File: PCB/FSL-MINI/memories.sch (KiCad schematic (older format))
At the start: 27 parts, among them J1001 SD CARD, Q1001 FDN340P, U1001 S25FL032P0XMFI013, U1002 24AA1025, U1003 24AA025E48

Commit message: Primer recorte realizado con Esteban Volentini <evolentini@gmail.com>.
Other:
- note added: "AVERIGUAR PROPOSITO"
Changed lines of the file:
@@
 $Descr A4 11693 8268
 encoding utf-8
-Sheet 10 13
+Sheet 5 6
 Title "CIAA Memorias NV"
 Date "2 dec 2014"
@@
 	1    0    0    -1
 $EndComp
-Text Notes 2000 7250 0    60   ~ 0
+Text Notes 2000 7400 0    60   ~ 0
 Detección de la memoria: Como el zócalo \nno posee switch mecánico, se utiliza \nun cambio de nivel en la línea DAT3,\npara lo cual es necesario un pull down\n(el valor 750k es el recomendado por FSL).
 $Comp
@@
 Connection ~ 2900 5500
 Wire Notes Line
-	1950 7100 4050 7100
+	1950 6900 4050 6900
 Wire Notes Line
-	4050 7100 4050 7650
+	4050 6900 4050 7450
 Wire Notes Line
-	1950 7100 1950 7650
+	1950 6900 1950 7450
 Wire Notes Line
-	1950 7650 4050 7650
+	1950 7450 4050 7450
+Text Notes 3650 2900 0    60   ~ 0
+AVERIGUAR PROPOSITO
+Text Notes 8150 6350 0    60   ~ 0
+AVERIGUAR PROPOSITO
 $EndSCHEMATC

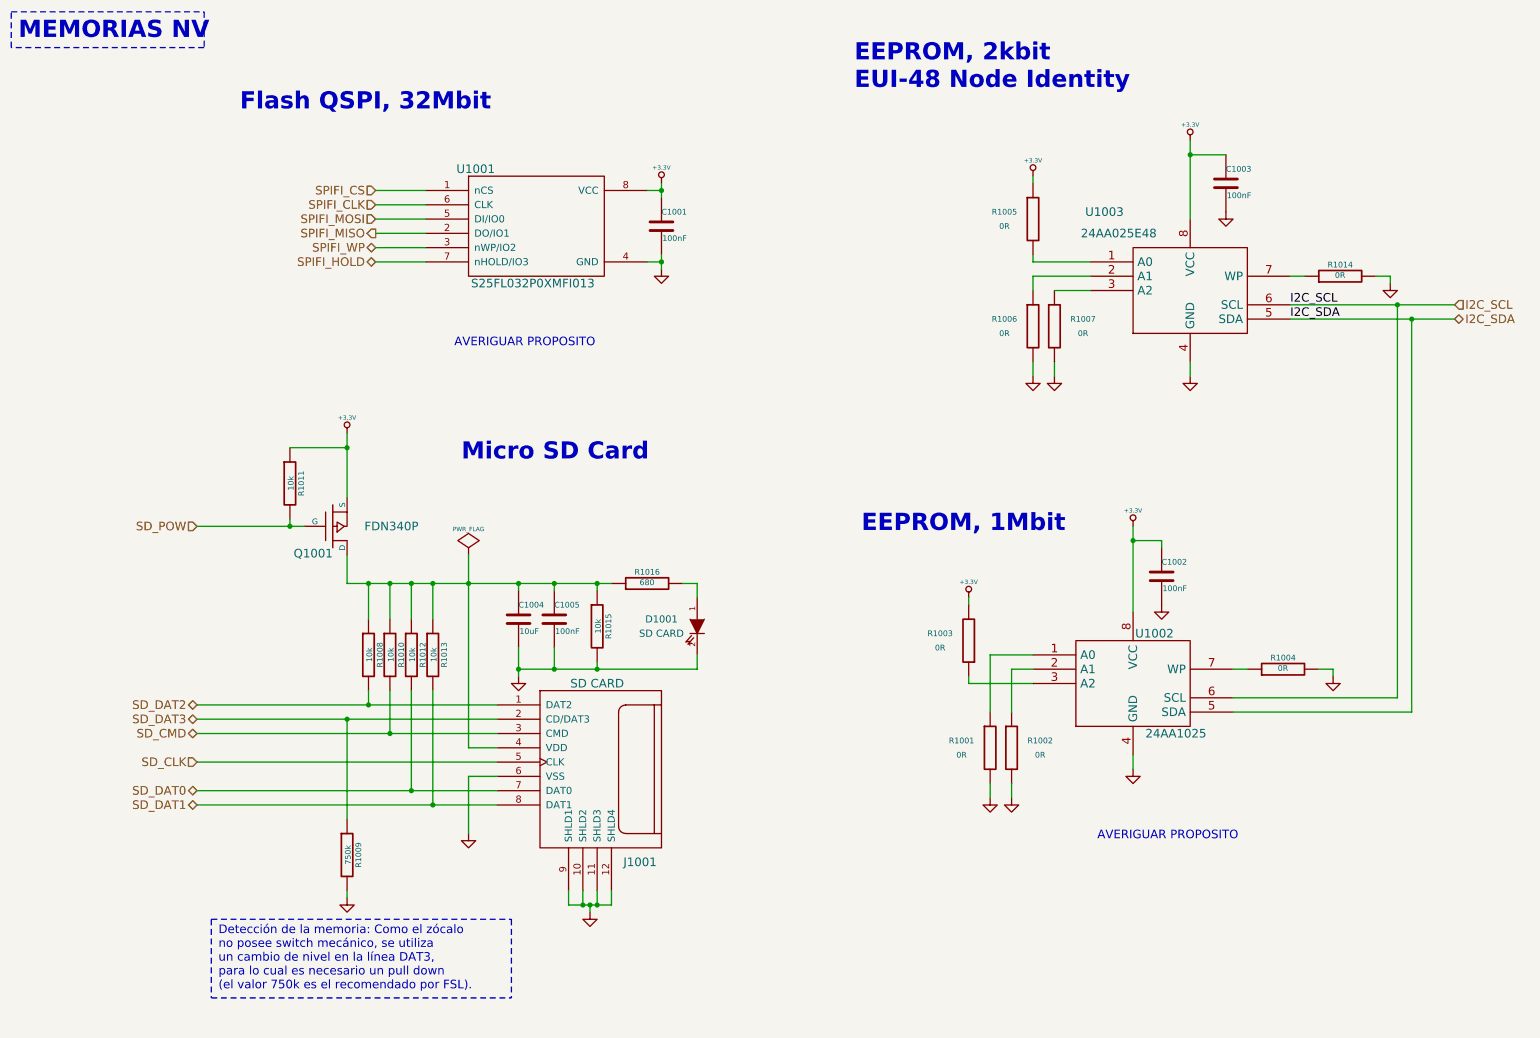
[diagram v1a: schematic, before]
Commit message: Added temporal connectors to avoid ERC.
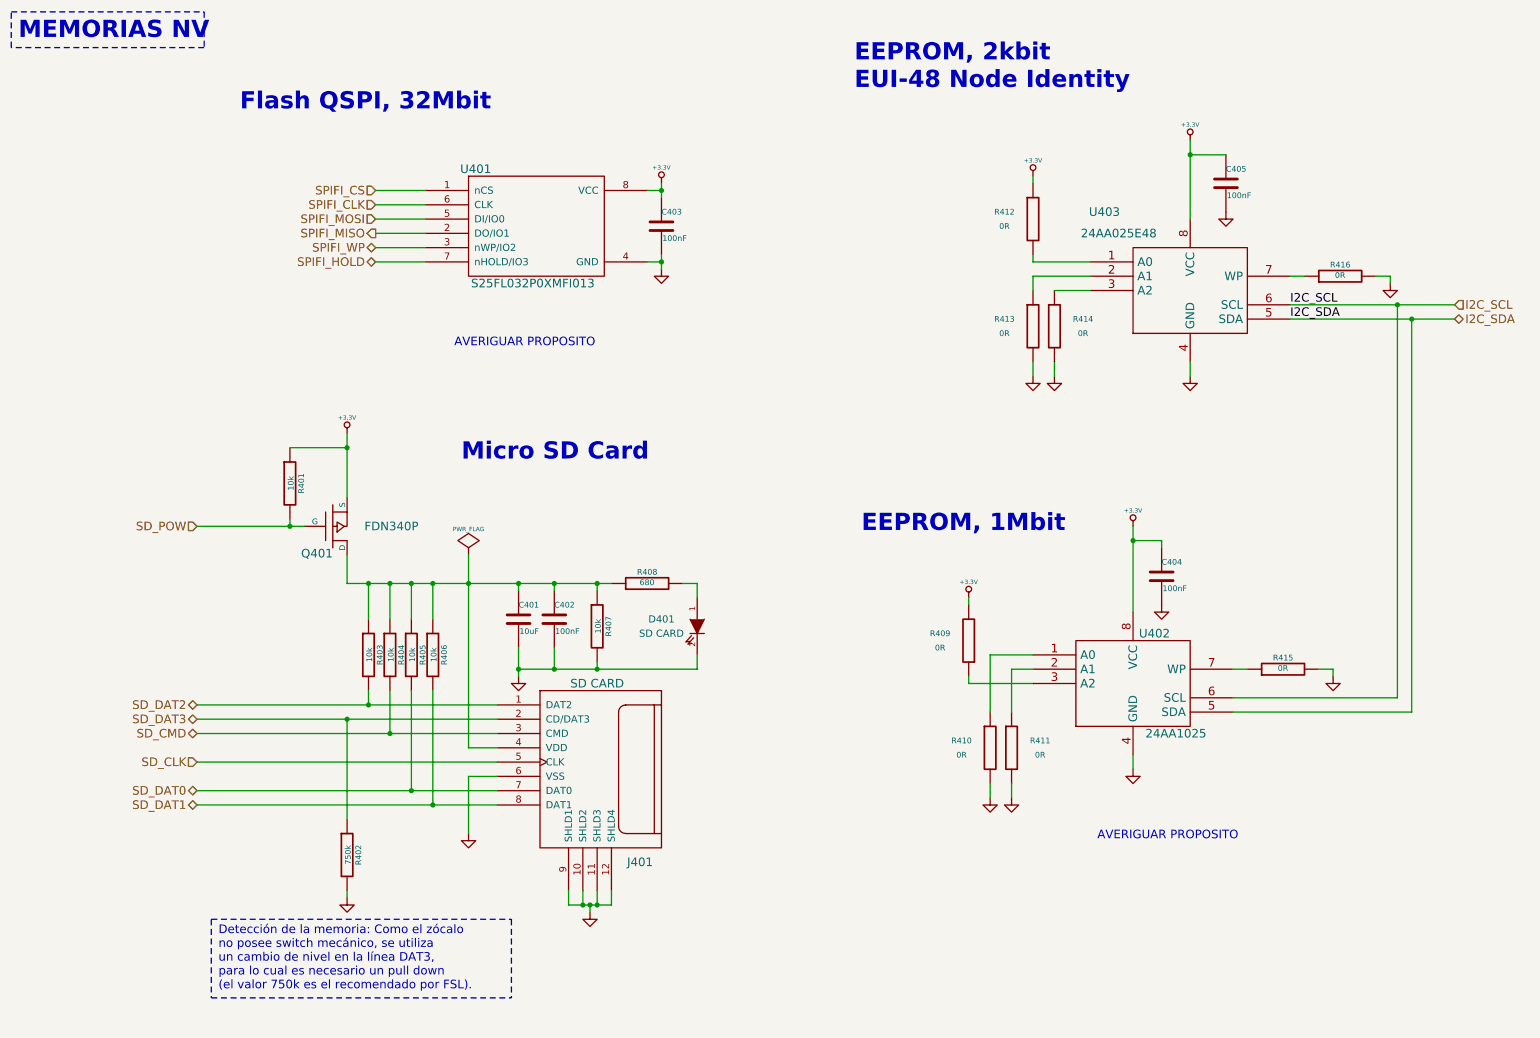
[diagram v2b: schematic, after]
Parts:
- renumbered C1004 to C401, C1005 to C402, C1001 to C403, C1002 to C404, C1003 to C405, D1001 to D401, J1001 to J401, Q1001 to Q401, R1011 to R401, R1009 to R402, R1008 to R403, R1010 to R404, R1012 to R405, R1013 to R406, R1015 to R407, R1016 to R408, R1003 to R409, R1001 to R410, R1002 to R411, R1005 to R412, R1006 to R413, R1007 to R414, R1004 to R415, R1014 to R416, U1001 to U401, U1002 to U402, U1003 to U403

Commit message: Footprint information in schematics.
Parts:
- C401: footprint c_1206POL -> footprints:c_1206POL
- C402, C403, C404, C405: footprint c_0603 -> footprints:c_0603
- D401: footprint LED-0603 -> footprints:LED-0603
- J401: footprint MicroSD_Hinged -> footprints:MicroSD_Hinged
- Q401: footprint SOT-23 -> footprints:SOT-23
- R401, R402, R403, R404, R405, R406, R407, R408, R409, R410, R411, R412, R413, R414, R415, R416: footprint r_0603 -> footprints:r_0603
- U401: footprint SOIC-8_WIDE -> footprints:SOIC-8_WIDE
- U402, U403: footprint SOIC-8 -> footprints:SOIC-8
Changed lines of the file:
@@
 F 0 "R403" V 3130 5050 40  0000 C CNN
 F 1 "10k" V 3057 5051 40  0000 C CNN
-F 2 "r_0603" H 3580 5050 30  0001 C CNN
+F 2 "footprints:r_0603" H 3580 5050 30  0001 C CNN
 F 3 "~" H 3650 5050 30  0000 C CNN
 F 4 "RES 10K OHM 1/10W 5% 0603 SMD" H 3650 5050 60  0001 C CNN "Descripcion"
@@
 F 0 "R404" V 3280 5050 40  0000 C CNN
 F 1 "10k" V 3207 5051 40  0000 C CNN
-F 2 "r_0603" H 3430 5050 30  0001 C CNN
+F 2 "footprints:r_0603" H 3430 5050 30  0001 C CNN
 F 3 "~" H 3500 5050 30  0000 C CNN
 F 4 "RES 10K OHM 1/10W 5% 0603 SMD" H 3500 5050 60  0001 C CNN "Descripcion"
@@
 F 0 "R405" V 3430 5050 40  0000 C CNN
 F 1 "10k" V 3357 5051 40  0000 C CNN
-F 2 "r_0603" H 3430 5050 30  0001 C CNN
+F 2 "footprints:r_0603" H 3430 5050 30  0001 C CNN
 F 3 "~" H 3500 5050 30  0000 C CNN
 F 4 "RES 10K OHM 1/10W 5% 0603 SMD" H 3500 5050 60  0001 C CNN "Descripcion"
@@
 F 0 "Q401" H 2800 4340 60  0000 R CNN
 F 1 "FDN340P" H 3400 4150 60  0000 R CNN
-F 2 "SOT-23" H 2800 4150 60  0001 C CNN
+F 2 "footprints:SOT-23" H 2800 4150 60  0001 C CNN
 F 3 "~" H 2800 4150 60  0000 C CNN
 F 4 "MOSFET P-CH 20V 2A SSOT3" H 2800 4150 60  0001 C CNN "Descripcion"
@@
 F 0 "R401" V 2580 3850 40  0000 C CNN
 F 1 "10k" V 2507 3851 40  0000 C CNN
-F 2 "r_0603" H 2580 4900 30  0001 C CNN
+F 2 "footprints:r_0603" H 2580 4900 30  0001 C CNN
 F 3 "~" H 2650 4900 30  0000 C CNN
 F 4 "RES 10K OHM 1/10W 5% 0603 SMD" H 2650 4900 60  0001 C CNN "Descripcion"
@@
 F 0 "R408" V 5080 4550 40  0000 C CNN
 F 1 "680" V 5007 4551 40  0000 C CNN
-F 2 "r_0603" V 4930 4550 30  0001 C CNN
+F 2 "footprints:r_0603" V 4930 4550 30  0001 C CNN
 F 3 "~" H 5000 4550 30  0000 C CNN
 F 4 "RES 680 OHM 1/10W 5% 0603 SMD" H 5000 4550 60  0001 C CNN "Descripcion"
@@
 F 0 "R407" V 4730 4850 40  0000 C CNN
 F 1 "10k" V 4657 4851 40  0000 C CNN
-F 2 "r_0603" H 3430 5050 30  0001 C CNN
+F 2 "footprints:r_0603" H 3430 5050 30  0001 C CNN
 F 3 "~" H 3500 5050 30  0000 C CNN
 F 4 "RES 10K OHM 1/10W 5% 0603 SMD" H 3500 5050 60  0001 C CNN "Descripcion"
@@
 F 0 "C402" H 4350 4900 40  0000 L CNN
 F 1 "100nF" H 4356 4715 40  0000 L CNN
-F 2 "c_0603" H 4388 4650 30  0001 C CNN
+F 2 "footprints:c_0603" H 4388 4650 30  0001 C CNN
 F 3 "~" H 4350 4800 60  0000 C CNN
 F 4 "CAP CER 0,1UF 16V 10% X7R 0603" H 4350 4800 60  0001 C CNN "Descripcion"
@@
 F 0 "C401" H 4100 4900 40  0000 L CNN
 F 1 "10uF" H 4106 4715 40  0000 L CNN
-F 2 "c_1206POL" H 4138 4650 30  0001 C CNN
+F 2 "footprints:c_1206POL" H 4138 4650 30  0001 C CNN
 F 3 "~" H 4100 4800 60  0000 C CNN
 F 4 "CAP TANT 10UF 6.3V 10% 1206" H 4100 4800 60  0001 C CNN "Descripcion"
@@
 F 0 "D401" V 5300 4600 50  0000 C CNN
 F 1 "SD CARD" V 5400 4600 50  0000 C CNN
-F 2 "LED-0603" H 5350 4850 60  0001 C CNN
+F 2 "footprints:LED-0603" H 5350 4850 60  0001 C CNN
 F 3 "~" H 5350 4850 60  0000 C CNN
 F 4 "LED GRN WATER CLEAR 0603 SMD" H 5350 4850 60  0001 C CNN "Descripcion"
@@
 F 0 "R406" V 3580 5050 40  0000 C CNN
 F 1 "10k" V 3507 5051 40  0000 C CNN
-F 2 "r_0603" H 3430 5050 30  0001 C CNN
+F 2 "footprints:r_0603" H 3430 5050 30  0001 C CNN
 F 3 "~" H 3500 5050 30  0000 C CNN
 F 4 "RES 10K OHM 1/10W 5% 0603 SMD" H 3500 5050 60  0001 C CNN "Descripcion"
@@
 F 0 "J401" H 4950 5300 60  0000 C CNN
 F 1 "SD CARD" H 4650 6550 60  0000 C CNN
-F 2 "MicroSD_Hinged" H 4650 5900 60  0001 C CNN
+F 2 "footprints:MicroSD_Hinged" H 4650 5900 60  0001 C CNN
 F 3 "~" H 4650 5900 60  0000 C CNN
 F 4 "CONN MEMORY CARD R/A 8POS SMD" H 4650 5900 60  0001 C CNN "Descripcion"
@@
 F 0 "U402" H 8550 5600 60  0000 C CNN
 F 1 "24AA1025" H 8700 4900 60  0000 C CNN
-F 2 "SOIC-8" H 8400 5250 60  0001 C CNN
+F 2 "footprints:SOIC-8" H 8400 5250 60  0001 C CNN
 F 3 "~" H 8400 5250 60  0000 C CNN
 F 4 "IC EEPROM 1MBIT 400KHZ 8SOIC" H 8400 5250 60  0001 C CNN "Descripcion"
@@
 F 0 "U403" H 8200 3050 60  0000 C CNN
 F 1 "24AA025E48" H 8300 2900 60  0000 C CNN
-F 2 "SOIC-8" H 8800 2500 60  0001 C CNN
+F 2 "footprints:SOIC-8" H 8800 2500 60  0001 C CNN
 F 3 "~" H 8800 2500 60  0000 C CNN
 F 4 "IC EEPROM 2KBIT 400KHZ 8SOIC" H 8800 2500 60  0001 C CNN "Descripcion"
@@
 F 0 "R411" H 7750 5750 40  0000 C CNN
 F 1 "0R" H 7750 5650 40  0000 C CNN
-F 2 "r_0603" V 11080 5800 30  0001 C CNN
+F 2 "footprints:r_0603" V 11080 5800 30  0001 C CNN
 F 3 "~" H 11150 5800 30  0000 C CNN
 F 4 "RES 0.0 OHM 1/10W JUMP 0603 SMD" H 11150 5800 60  0001 C CNN "Descripcion"
@@
 F 0 "R409" H 7450 4900 40  0000 C CNN
 F 1 "0R" H 7450 5000 40  0000 C CNN
-F 2 "r_0603" V 10630 5050 30  0001 C CNN
+F 2 "footprints:r_0603" V 10630 5050 30  0001 C CNN
 F 3 "~" H 10700 5050 30  0000 C CNN
 F 4 "RES 0.0 OHM 1/10W JUMP 0603 SMD" H 10700 5050 60  0001 C CNN "Descripcion"
@@
 F 0 "R410" H 7200 5750 40  0000 C CNN
 F 1 "0R" H 7200 5650 40  0000 C CNN
-F 2 "r_0603" V 11080 5800 30  0001 C CNN
+F 2 "footprints:r_0603" V 11080 5800 30  0001 C CNN
 F 3 "~" H 11150 5800 30  0000 C CNN
 F 4 "RES 0.0 OHM 1/10W JUMP 0603 SMD" H 11150 5800 60  0001 C CNN "Descripcion"
@@
 F 0 "R413" H 7500 2800 40  0000 C CNN
 F 1 "0R" H 7500 2700 40  0000 C CNN
-F 2 "r_0603" V 7780 2750 30  0001 C CNN
+F 2 "footprints:r_0603" V 7780 2750 30  0001 C CNN
 F 3 "~" H 7850 2750 30  0000 C CNN
 F 4 "RES 0.0 OHM 1/10W JUMP 0603 SMD" H 7850 2750 60  0001 C CNN "Descripcion"
@@
 F 0 "R414" H 8050 2800 40  0000 C CNN
 F 1 "0R" H 8050 2700 40  0000 C CNN
-F 2 "r_0603" V 7780 2750 30  0001 C CNN
+F 2 "footprints:r_0603" V 7780 2750 30  0001 C CNN
 F 3 "~" H 7850 2750 30  0000 C CNN
 F 4 "RES 0.0 OHM 1/10W JUMP 0603 SMD" H 7850 2750 60  0001 C CNN "Descripcion"
@@
 F 0 "R412" H 7500 2050 40  0000 C CNN
 F 1 "0R" H 7500 1950 40  0000 C CNN
-F 2 "r_0603" V 7930 2000 30  0001 C CNN
+F 2 "footprints:r_0603" V 7930 2000 30  0001 C CNN
 F 3 "~" H 8000 2000 30  0000 C CNN
 F 4 "RES 0.0 OHM 1/10W JUMP 0603 SMD" H 8000 2000 60  0001 C CNN "Descripcion"
@@
 F 0 "R415" V 9530 5150 40  0000 C CNN
 F 1 "0R" V 9457 5151 40  0000 C CNN
-F 2 "r_0603" V 11180 5850 30  0001 C CNN
+F 2 "footprints:r_0603" V 11180 5850 30  0001 C CNN
 F 3 "~" H 11250 5850 30  0001 C CNN
 F 4 "RES 0.0 OHM 1/10W JUMP 0603 SMD" H 11250 5850 60  0001 C CNN "Descripcion"
@@
 F 0 "R416" V 9930 2400 40  0000 C CNN
 F 1 "0R" V 9857 2401 40  0000 C CNN
-F 2 "r_0603" V 8130 3000 30  0001 C CNN
+F 2 "footprints:r_0603" V 8130 3000 30  0001 C CNN
 F 3 "~" H 8200 3000 30  0000 C CNN
 F 4 "RES 0.0 OHM 1/10W JUMP 0603 SMD" H 8200 3000 60  0001 C CNN "Descripcion"
@@
 F 0 "C405" H 9050 1850 40  0000 L CNN
 F 1 "100nF" H 9056 1665 40  0000 L CNN
-F 2 "c_0603" H 9288 4800 30  0001 C CNN
+F 2 "footprints:c_0603" H 9288 4800 30  0001 C CNN
 F 3 "~" H 9250 4950 60  0000 C CNN
 F 4 "CAP CER 0,1UF 16V 10% X7R 0603" H 9250 4950 60  0001 C CNN "Descripcion"
@@
 F 0 "C404" H 8600 4600 40  0000 L CNN
 F 1 "100nF" H 8606 4415 40  0000 L CNN
-F 2 "c_0603" H 12338 7650 30  0001 C CNN
+F 2 "footprints:c_0603" H 12338 7650 30  0001 C CNN
 F 3 "~" H 12300 7800 60  0000 C CNN
 F 4 "CAP CER 0,1UF 16V 10% X7R 0603" H 12300 7800 60  0001 C CNN "Descripcion"
@@
 F 0 "U401" H 3800 2450 60  0000 C CNN
 F 1 "S25FL032P0XMFI013" H 4200 1650 60  0000 C CNN
-F 2 "SOIC-8_WIDE" H 4200 1850 60  0001 C CNN
+F 2 "footprints:SOIC-8_WIDE" H 4200 1850 60  0001 C CNN
 F 3 "~" H 4200 1850 60  0000 C CNN
 F 4 "IC NOR FLASH 32MBIT 104MHZ" H 4200 2050 60  0001 C CNN "Descripcion"
@@
 F 0 "C403" H 5100 2150 40  0000 L CNN
 F 1 "100nF" H 5106 1965 40  0000 L CNN
-F 2 "c_0603" H 5338 5100 30  0001 C CNN
+F 2 "footprints:c_0603" H 5338 5100 30  0001 C CNN
 F 3 "~" H 5300 5250 60  0000 C CNN
 F 4 "CAP CER 0,1UF 16V 10% X7R 0603" H 5300 5250 60  0001 C CNN "Descripcion"
@@
 F 0 "R402" V 2980 6450 40  0000 C CNN
 F 1 "750k" V 2907 6451 40  0000 C CNN
-F 2 "r_0603" H 3430 6450 30  0001 C CNN
+F 2 "footprints:r_0603" H 3430 6450 30  0001 C CNN
 F 3 "~" H 3500 6450 30  0000 C CNN
 F 4 "RES 750K OHM 1/10W 5% 0603 SMD" H 3500 6450 60  0001 C CNN "Descripcion"

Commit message: Swap ethernet schematic sheet for CIAA NXP ethernet sheet. Preliminary schematic finished. Add notas.txt file.
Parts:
- C401: footprint footprints:c_1206POL -> FSL-MINI:c_1206POL
- C402, C403, C404, C405: footprint footprints:c_0603 -> FSL-MINI:c_0603
- D401: footprint footprints:LED-0603 -> FSL-MINI:LED-0603
- J401: footprint footprints:MicroSD_Hinged -> FSL-MINI:MicroSD_Hinged
- Q401: footprint footprints:SOT-23 -> FSL-MINI:SOT-23
- R401, R402, R403, R404, R405, R406, R407, R408, R409, R410, R411, R412, R413, R414, R415, R416: footprint footprints:r_0603 -> FSL-MINI:r_0603
- U401: footprint footprints:SOIC-8_WIDE -> FSL-MINI:SOIC-8_WIDE
- U402, U403: footprint footprints:SOIC-8 -> FSL-MINI:SOIC-8
